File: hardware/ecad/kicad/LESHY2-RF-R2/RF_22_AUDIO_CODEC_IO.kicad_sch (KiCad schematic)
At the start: 118 parts, among them U66 TLV9061IDBVR, U67 Texas Instruments TS5A63157DC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, U68 Texas Instruments SN74LVC1G31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, U69 Texas Instruments SN74LVC2G08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, U70 Texas Instruments TMUX1136DGSR, U71 Texas Instruments TS5A63157DC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, U72 Everest Semiconductor ES8311, U73 Texas Instruments SN74LVC2G66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, U74 Texas Instruments SN74LVC1G12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, U75 SN74LVC1G08DCKR, U76 Texas Instruments SN74LVC1G12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, U77 Texas Instruments SN74LVC1G12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, U78 Texas Instruments SN74LVC1G12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, U79 Texas Instruments TPS22919DCKR, U80 Texas Instruments TPS3839K33D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, U81 Texas Instruments TPD4E05U06D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, U82 Same Sky SJ-43504-SMT-TR, U83 TCA9534APWR, U84 Texas Instruments TS5A63157DC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, U85 Diodes Incorporated PAM8302AA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

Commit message: Verify factory-placeable Airband filter
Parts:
- renumbered C190 to C189, C191 to C190, C192 to C191, C193 to C192, C194 to C193, C195 to C194, C196 to C195, C197 to C196, C198 to C197, C199 to C198, C200 to C199, C201 to C200, C202 to C201, C203 to C202, C204 to C203, C205 to C204, C206 to C205, C207 to C206, C208 to C207, C209 to C208, C210 to C209, C211 to C210, C212 to C211, C213 to C212, C214 to C213, C215 to C214, C216 to C215, C217 to C216, C218 to C217, C219 to C218, C220 to C219, C221 to C220, C222 to C221, C223 to C222, C224 to C223, C225 to C224, C226 to C225, C227 to C226, C228 to C227, C229 to C228, C230 to C229, C231 to C230, C232 to C231, C233 to C232, C234 to C233, C235 to C234, L30 to L29, L31 to L30, L32 to L31, L33 to L32

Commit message: Complete current R2 schematic and sourcing revalidation
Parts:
- renumbered C189 to C194, C190 to C195, C191 to C196, C192 to C197, C193 to C198, C194 to C199, C195 to C200, C196 to C201, C197 to C202, C198 to C203, C199 to C204, C200 to C205, C201 to C206, C202 to C207, C203 to C208, C204 to C209, C205 to C210, C206 to C211, C207 to C212, C208 to C213, C209 to C214, C210 to C215, C211 to C216, C212 to C217, C213 to C218, C214 to C219, C215 to C220, C216 to C221, C217 to C222, C218 to C223, C219 to C224, C220 to C225, C221 to C226, C222 to C227, C223 to C228, C224 to C229, C225 to C230, C226 to C231, C227 to C232, C228 to C233, C229 to C234, C230 to C235, C231 to C236, C232 to C237, C233 to C238, C234 to C239, L29 to L28, L30 to L29, L31 to L30, L32 to L31, R165 to R166, R166 to R167, R167 to R168, R168 to R169, R169 to R170, R170 to R171, R171 to R172, R172 to R173, R173 to R174, R174 to R175, R175 to R176, R176 to R177, R177 to R178, R178 to R179, R179 to R180, R180 to R181, R181 to R182, R182 to R183, R183 to R184, R184 to R185, R185 to R186, R186 to R187, R187 to R188, R188 to R189, R189 to R190, R190 to R191, R191 to R192, R192 to R193, R193 to R194, R194 to R195, R195 to R196, R196 to R197, R197 to R198, R198 to R199, R199 to R200, R200 to R201, R201 to R202, R202 to R203, R203 to R204, R204 to R205, R205 to R206, R206 to R207, R207 to R208, R208 to R209, R209 to R210, R210 to R211, U66 to U67, U67 to U68, U68 to U69, U69 to U70, U70 to U71, U71 to U72, U72 to U73, U73 to U74, U74 to U75, U75 to U76, U76 to U77, U77 to U78, U78 to U79, U79 to U80, U80 to U81, U81 to U82, U82 to U83, U83 to U84, U84 to U85, U85 to U86

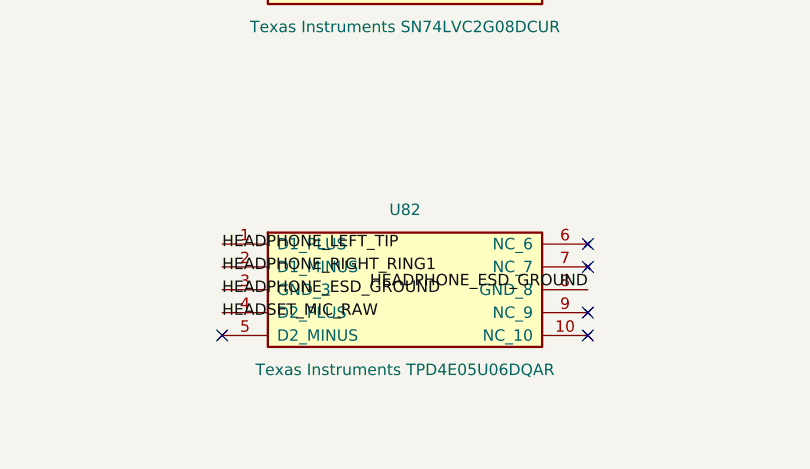
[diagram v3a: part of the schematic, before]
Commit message: Canonicalize physical ground anchors
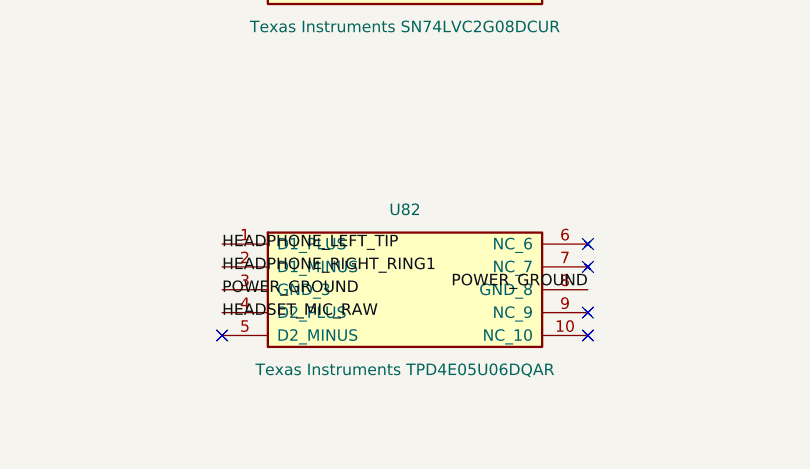
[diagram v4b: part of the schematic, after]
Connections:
- net HEADPHONE_ESD_GROUND is gone; now on net POWER_GROUND: U82.3 (GND_3), U82.8 (GND_8)
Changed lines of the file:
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@@
 		(effects (font (size 1.27 1.27)))
 	)
-	(label "HEADPHONE_ESD_GROUND"
+	(label "POWER_GROUND"
 		(at 492.76 373.38 0)
 		(effects (font (size 1.27 1.27)))
@@
 	(no_connect (at 533.40 370.84)
 	)
-	(label "HEADPHONE_ESD_GROUND"
+	(label "POWER_GROUND"
 		(at 533.40 373.38 180)
 		(effects (font (size 1.27 1.27)) (justify right bottom))

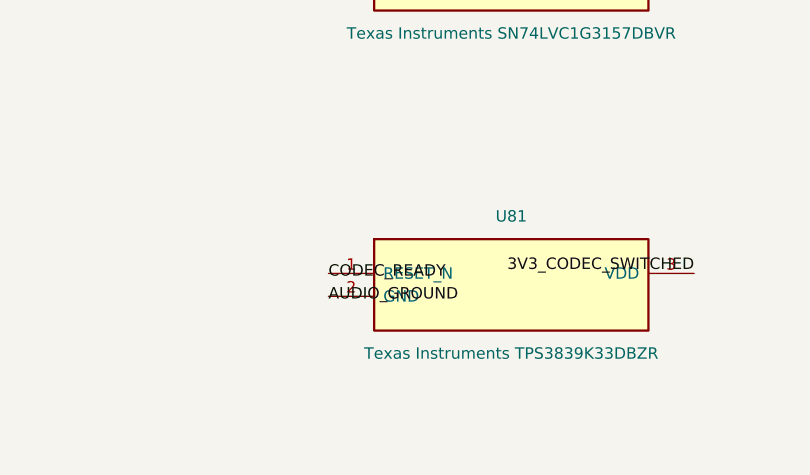
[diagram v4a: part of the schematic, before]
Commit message: Correct exact connector and protection geometry; expand electrical review
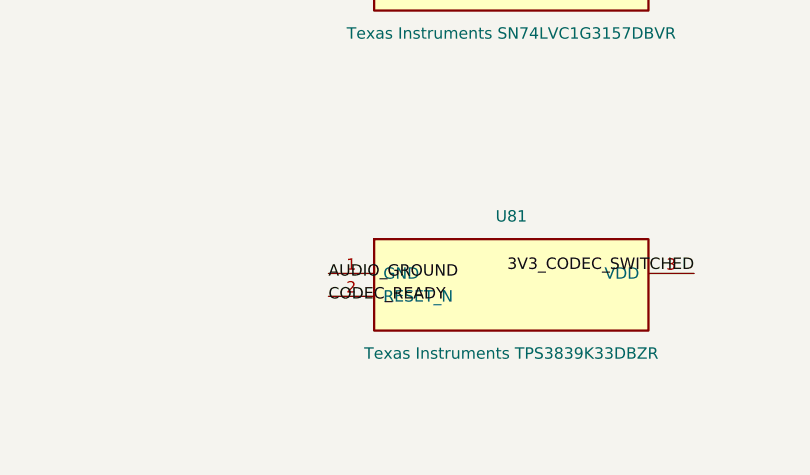
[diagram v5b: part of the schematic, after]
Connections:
- net AUDIO_GROUND: now also U81.1 (GND); no longer U81.2 (GND)
- net CODEC_READY: now also U81.2 (RESET_N); no longer U81.1 (RESET_N)
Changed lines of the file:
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@@
 		)
 	)
-	(label "CODEC_READY"
+	(label "AUDIO_GROUND"
 		(at 401.32 370.84 0)
 		(effects (font (size 1.27 1.27)))
 	)
-	(label "AUDIO_GROUND"
+	(label "CODEC_READY"
 		(at 401.32 373.38 0)
 		(effects (font (size 1.27 1.27)))

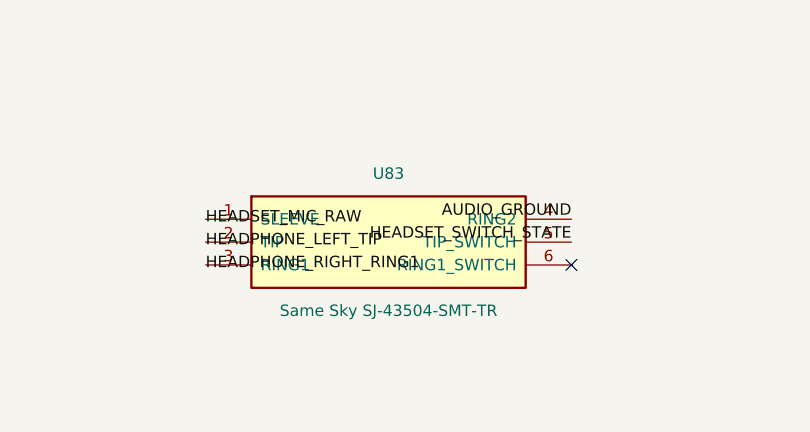
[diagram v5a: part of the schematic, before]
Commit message: Integrate reviewed R2 interface geometry and refresh guarded PCB evidence
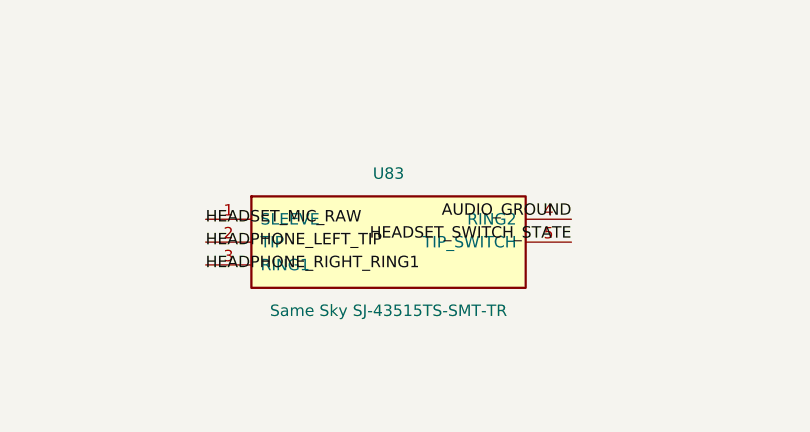
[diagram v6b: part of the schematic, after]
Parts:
- U83: value Same Sky SJ-43504-SMT-TR -> Same Sky SJ-43515TS-SMT-TR; footprint Leshy2:SJ-43504-SMT-TR -> Leshy2_R2:SJ-43515TS-SMT-TR; symbol Leshy2_R2:same_sky_sj_43504_smt_tr -> Leshy2_R2:same_sky_sj_43515ts_smt_tr
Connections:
- no-connect marks 9 -> 8
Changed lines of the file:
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@@
 	)
 	(symbol
-		(lib_id "Leshy2_R2:same_sky_sj_43504_smt_tr")
+		(lib_id "Leshy2_R2:same_sky_sj_43515ts_smt_tr")
 		(at 695.96 372.11 0)
 		(unit 1)
@@
 			(effects (font (size 1.27 1.27)))
 		)
-		(property "Value" "Same Sky SJ-43504-SMT-TR"
+		(property "Value" "Same Sky SJ-43515TS-SMT-TR"
 			(at 695.96 379.73 0)
 			(show_name no)
@@
 			(effects (font (size 1.27 1.27)))
 		)
-		(property "Footprint" "Leshy2:SJ-43504-SMT-TR"
+		(property "Footprint" "Leshy2_R2:SJ-43515TS-SMT-TR"
 			(at 695.96 372.11 0)
 			(show_name no)
@@
 			(effects (font (size 1.27 1.27)))
 		)
-		(property "Description" "same_sky_sj_43504_smt_tr"
+		(property "Description" "same_sky_sj_43515ts_smt_tr"
 			(at 695.96 372.11 0)
 			(show_name no)
@@
 		)
 		(pin "5"
-		)
-		(pin "6"
 		)
 		(instances
@@
 		(effects (font (size 1.27 1.27)) (justify right bottom))
 	)
-	(no_connect (at 716.28 374.65)
-	)
 	(symbol
